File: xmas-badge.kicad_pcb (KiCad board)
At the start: 2 copper layers, 94 x 62.2 mm, 16 parts, among them U1 LP, U2 LP, U3 LP, U4 LP, U5 LP, U6 LP, U7 BAT_HLD_2032

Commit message: first small version
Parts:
- removed D1: LED, LED_THT:LED_D5.0mm
- removed the G*** at (111.8, 111.8)
- removed R1, R2, R3, R4, R5, R6: R, Resistor_THT:R_Axial_DIN0411_L9.9mm_D3.6mm_P12.70mm_Horizontal
- removed S1: Micro_Schalter, KHF_LIB:Micro_SchalterKHF
- removed U1, U2, U3, U4, U5, U6: LP, KHF_LIB:LP
- removed U7: BAT_HLD_2032, Battery:BatteryHolder_Keystone_106_1x20mm
- added  : MountingHole_2.2mm_M2, MountingHole:MountingHole_2.2mm_M2, F.Cu at (151.9, 79.5)
- added G*** (x4): LOGO, LOGO, F.Cu at (0.00, 0.00)
- added G*** (x3): LOGO, LOGO, F.Cu at (151.9, 98.0)
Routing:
- net Net-(D1-Pad1): track 58.0 -> 0.00 mm
- net Net-(R1-Pad2): track 51.8 -> 0.00 mm
- net Net-(S1-Pad1): track 38.1 -> 0.00 mm
- net Net-(R4-Pad2): track 31.2 -> 0.00 mm
- net Net-(R4-Pad1): track 28.0 -> 0.00 mm
- net Net-(R1-Pad1): track 27.3 -> 0.00 mm
- net Net-(D1-Pad2): track 12.1 -> 0.00 mm
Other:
- board size 94 x 62.2 mm -> 38.1 x 42.4 mm
- net class Default: via_dia 0.8 -> 0.6
- rule pad_to_mask_clearance: 0 -> 0.2
- board text removed: "+Bat"
- board text removed: "-Bat"
- board text removed: "A"
- board text removed: "C"
- board text removed: "CR2032"
- board text removed: "Lötübung 01"

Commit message: saved
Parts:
- removed the G*** at (0.00, 0.00) (x4)
- removed the G*** at (151.9, 98.0) (x3)
- added D1: LED, LED_THT:LED_D5.0mm, B.Cu at (150.6, 115.7)
- added G*** (x4): LOGO, LOGO, F.Cu at (0.00, 0.00)
- added G*** (x3): LOGO, LOGO, F.Cu at (151.9, 98.0)
- added R1: R, Resistor_THT:R_Axial_DIN0411_L9.9mm_D3.6mm_P12.70mm_Horizontal, B.Cu at (160.2, 92.7)
- added R2: R, Resistor_THT:R_Axial_DIN0411_L9.9mm_D3.6mm_P12.70mm_Horizontal, B.Cu at (167.0, 102.2)
- added R3: R, Resistor_THT:R_Axial_DIN0411_L9.9mm_D3.6mm_P12.70mm_Horizontal, B.Cu at (145.5, 95.2)
- added R4: R, Resistor_THT:R_Axial_DIN0411_L9.9mm_D3.6mm_P12.70mm_Horizontal, B.Cu at (136.8, 102.4)
- added R5: R, Resistor_THT:R_Axial_DIN0411_L9.9mm_D3.6mm_P12.70mm_Horizontal, B.Cu at (140.7, 104.5)
- added R6: R, Resistor_THT:R_Axial_DIN0411_L9.9mm_D3.6mm_P12.70mm_Horizontal, B.Cu at (137.8, 106.0)
- added S1: Micro_Schalter, libraries:Micro_SchalterKHF, B.Cu at (159.0, 113.0)
- added U1: BAT_HLD_2032, libraries:BAT-HLD-012-SMT, B.Cu at (151.9, 87.8)
- added U2: LP, libraries:LP, B.Cu at (155.1, 95.2)
- added U3: LP, libraries:LP, B.Cu at (148.7, 95.2)
- added U4: LP, libraries:LP, F.Cu at (140.2, 96.9)
- added U5: LP, libraries:LP, F.Cu at (140.2, 99.5)

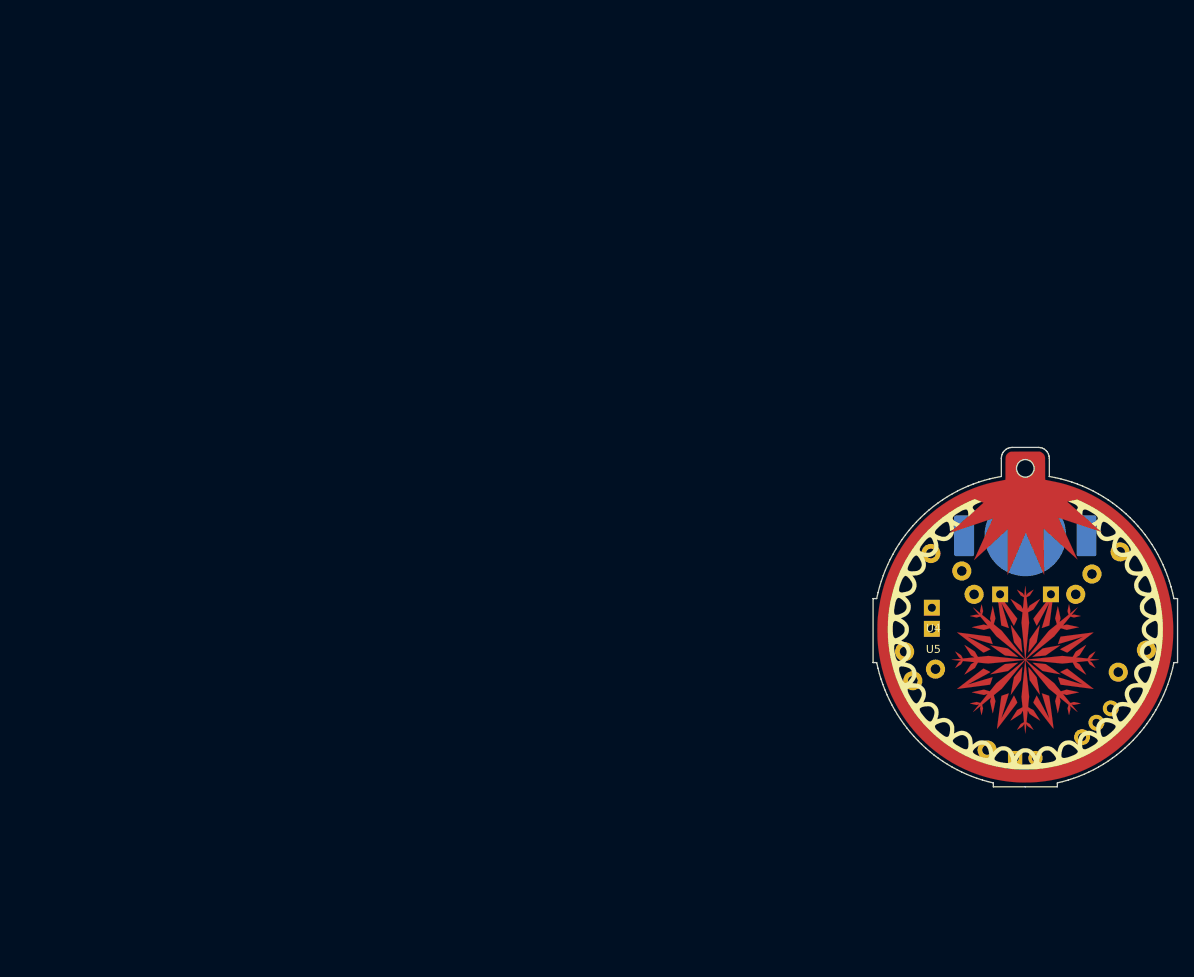
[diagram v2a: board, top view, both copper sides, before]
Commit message: increased size, component placement
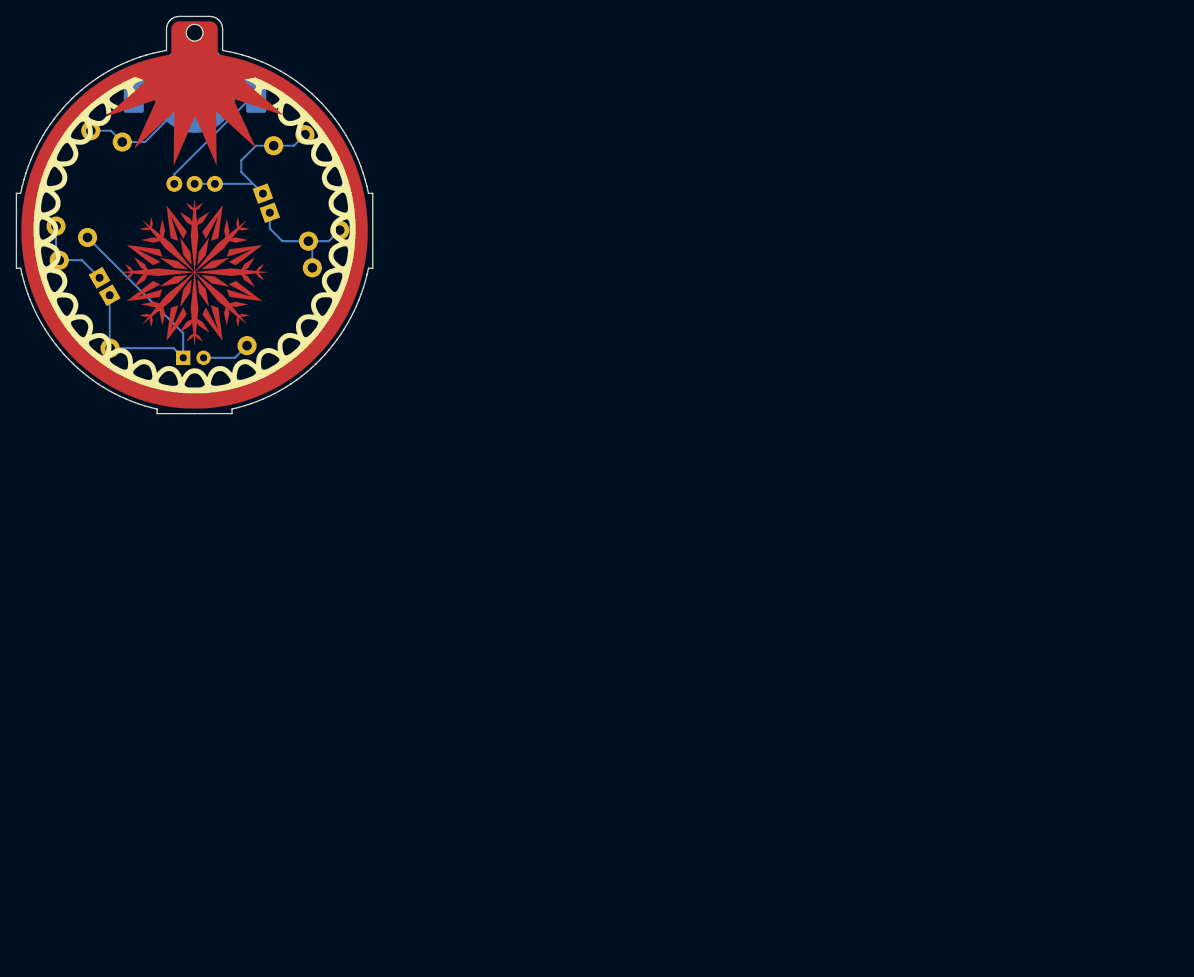
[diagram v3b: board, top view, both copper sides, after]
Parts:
- removed the   at (151.9, 79.5)
- removed the G*** at (0.00, 0.00) (x4)
- removed the G*** at (151.9, 98.0) (x3)
- removed U2, U3, U4, U5: LP, libraries:LP
- added  : MountingHole_2.1mm, MountingHole:MountingHole_2.1mm, F.Cu at (48.1, 25.0)
- added  : LP, libraries:LP, B.Cu at (36.2, 55.6)
- added  : LP, libraries:LP, F.Cu at (37.4, 57.8)
- added  : LP, libraries:LP, F.Cu at (56.6, 45.1)
- added  : LP, libraries:LP, F.Cu at (57.5, 47.5)
- added G*** (x4): LOGO, LOGO, F.Cu at (0.00, 0.00)
- added G*** (x3): LOGO, LOGO, F.Cu at (48.1, 47.6)
- moved R2 142.0 mm to (34.7, 50.6), turned to 70 degrees
- moved R1 136.6 mm to (30.7, 49.2), turned to 70 degrees
- moved S1 132.9 mm to (45.5, 43.9), turned to 0 degrees
- moved U1 117.7 mm to (48.1, 32.4)
- moved D1 115.4 mm to (46.6, 65.6)
- moved R3 112.3 mm to (37.5, 64.4), turned to 120 degrees
- moved R6 93.2 mm to (54.6, 64.1), turned to 50 degrees
- moved R5 92.5 mm to (66.2, 49.7), turned to 110 degrees
- moved R4 90.5 mm to (62.3, 51.1), turned to 110 degrees
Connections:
- U1 pad 1: Net-(S1-Pad1) -> Net-(R1-Pad2)
- U1 pad 2: Net-(R1-Pad2) -> Net-(S1-Pad1)
- U1 pad 3: (no net) -> Net-(S1-Pad1)
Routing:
- net Net-(D1-Pad1): track 0.00 -> 36.3 mm
- net Net-(S1-Pad1): track 0.00 -> 35.6 mm
- net Net-(R4-Pad2): track 0.00 -> 21.9 mm
- net Net-(R1-Pad2): track 0.00 -> 16.2 mm
- net Net-(R4-Pad1): track 0.00 -> 15.5 mm
- net Net-(R1-Pad1): track 0.00 -> 10.4 mm
- net Net-(D1-Pad2): track 0.00 -> 6.07 mm
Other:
- board size 38.1 x 42.4 mm -> 44.5 x 49.7 mm
- board text added: "+ Pol"
- board text added: "- Pol"
- board text added: "Karlheinz Frank Alexander Kutschera October 2021"
- board text added: "OBERLAB"
- board text added: "github.com/oberlab/xmas-badge"
